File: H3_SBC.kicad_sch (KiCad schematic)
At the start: 7 parts, among them U1 H3, U8 XOS32024000LT00351005, X1 X201232768KLD2SI

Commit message: changed some ethernet stuff
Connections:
- net PA20: now reaches U1.A13 (PA20)
- net PA21: now reaches U1.A14 (PA21)
- net PA18: now reaches U1.B13 (PA18)
- net PA19: now reaches U1.B14 (PA19)
- net TWI0_SDA: now reaches U1.C13 (PA12)
- net PA17: now reaches U1.C14 (PA17)
- net JTAG_MS: now reaches U1.D11 (PA0)
- net PA9: now reaches U1.D13 (PA9)
- net UART3_CTS: now reaches U1.D15 (PA16)
- net JTAG_CK: now reaches U1.D5 (PA1)
- net JTAG_DO: now reaches U1.D6 (PA2)
- net PA7: now reaches U1.D8 (PA7)
- net PA10: now reaches U1.E11 (PA10)
- net JTAG_DI: now reaches U1.E13 (PA3)
- net PA6: now reaches U1.E14 (PA6)
- net UART3_TX: now reaches U1.E15 (PA13)
- net TWI0_SCK: now reaches U1.F11 (PA11)
- net PA8: now reaches U1.F13 (PA8)
- net UART3_RTS: now reaches U1.F14 (PA15)
- net PA4: now reaches U1.F5 (PA4)
- net UART3_RX: now reaches U1.G12 (PA14)
- net PA5: now reaches U1.H6 (PA5)
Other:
- moved on the sheet: C23, C24, C25, C26, U1A, U8, X1

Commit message: power things, minor changes
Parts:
- added D1, D3: RED, symbol Device:LED
- added D2: YELLOW, symbol Device:LED
- added R14: 47K, symbol Device:R
- added R15: 100K, symbol Device:R
- added R16, R17, R18: 330R, symbol Device:R
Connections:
- net GND: now also R16.2
- net STATLED_DISK: now reaches U1.M6 (PL9)
- net STATLED_DISK: now also R17.2
- net STATLED_ERR: now reaches U1.V2 (PL10)
- net STATLED_ERR: now also R18.2
- net at U1.AA5 (KEYADC): now also R15.2
- net at U1.AA6 (NMI): now also R14.2
- net TVOUT: now reaches U1.F10 (TVOUT)
- net AXP_PWROK: now reaches U1.V6 (RESET)
- net UBOOT: now reaches U1.W6 (UBOOT)
- net EPHY_LINK_LED: no longer names the net of U1.A2 (EPHY_LINK_LE)
- net EPHY_SPD_LED: no longer names the net of U1.F7 (EPHY_SPD_LE)
- new net: D3.1 (K), R18.1
- new net: D1.1 (K), R16.1
- new net: D2.1 (K), R17.1
- new net VCC3V3: D1.2 (A), D2.2 (A), D3.2 (A)
- new net VCC_RTC: R14.1, R15.1
- no-connect marks 7 -> 23
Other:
- moved on the sheet: C23, C24, C25, C26, U1A, U8, X1

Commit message: small changes
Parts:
- added C66: 10uF, symbol Device:C
- added C67: 0.1uF, symbol Device:C
- added C68: 1uF, symbol Device:C
- added C69: 4.7uF, symbol Device:C
- added R19: 220K, symbol Device:R
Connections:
- net GND: now also C66.2, C67.2, C68.2, C69.2, R19.2
- net PG5: now reaches U1.C1 (PG5)
- net PG4: now reaches U1.C2 (PG4)
- net PG8: now reaches U1.C3 (PG8)
- net PG11: now reaches U1.D2 (PG11)
- net PG7: now reaches U1.D3 (PG7)
- net PG9: now reaches U1.E3 (PG9)
- net PG3: now reaches U1.F3 (PG3)
- net PG6: now reaches U1.G4 (PG6)
- net PG2: now reaches U1.H4 (PG2)
- net PG0: now reaches U1.J3 (PG0)
- net PG1: now reaches U1.L2 (PG1)
- net PG10: now reaches U1.M3 (PG10)
- net at U1.V4 (VRP): now also C66.1, C67.1
- net at U1.W5 (VRA2): now also C69.1, R19.1
- net at U1.Y4 (VRA1): now also C68.1
- no-connect marks 23 -> 24
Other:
- moved on the sheet: U1B

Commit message: minor changes
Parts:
- removed U8: XOS32024000LT00351005, easyeda2kicad:OSC-SMD_4P-L3.2-W2.5-BL, symbol easyeda2kicad:XOS32024000LT00351005
- added unit 7 of U1
- added X2: SMD-5032_4P 24M 20pf, easyeda2kicad:CRYSTAL-SMD_4P-L5.0-W3.2-BL, symbol easyeda2kicad:SMD-5032_4P24M20pf
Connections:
- net GND: now also X2.2 (GND), X2.4 (GND)
- net at C25.1, U1.K2 (X24MIN): now also X2.1 (OSC1)
- net at C26.1, U1.K1 (X24MOUT): now also X2.3 (OSC2)
- new net USB0_D+: U1.A5 (USB_DP0)
- new net USB0_D-: U1.B5 (USB_DM0)
- new net USB1_D+: U1.B6 (USB_DP1)
- new net USB1_D-: U1.B7 (USB_DM1)
- new net USB2_D+: U1.A7 (USB_DP2)
- new net USB2_D-: U1.A8 (USB_DM2)
- new net USB3_D+: U1.B8 (USB_DP3)
- new net USB3_D-: U1.B9 (USB_DM3)
- no-connect marks 24 -> 40
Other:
- moved on the sheet: C23, C24, C25, C26, C66, C67, C68, C69, D1, D2, D3, R14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

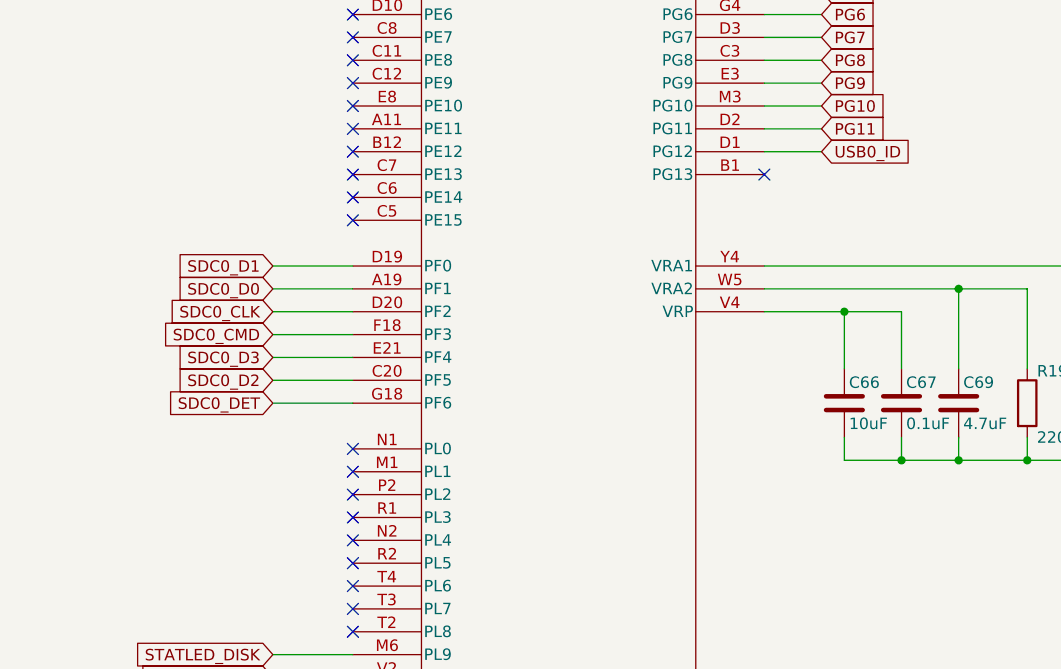
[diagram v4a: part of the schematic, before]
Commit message: recovered ethernet power changes
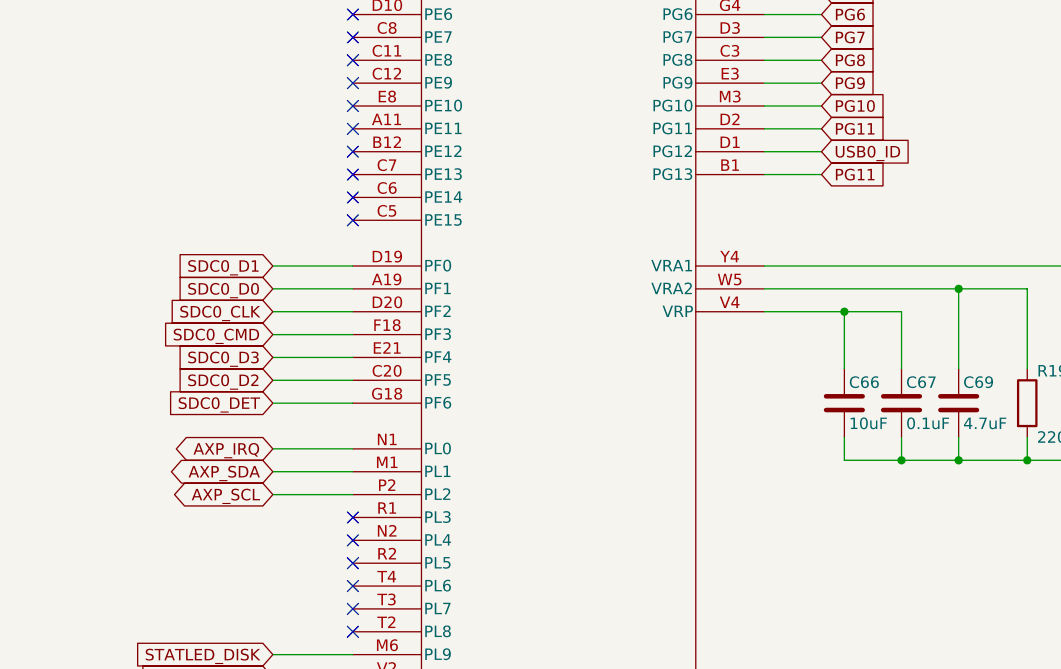
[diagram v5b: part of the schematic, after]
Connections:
- net PG11: now also U1.B1 (PG13)
- net AXP_SDA: now reaches U1.M1 (PL1)
- net AXP_IRQ: now reaches U1.N1 (PL0)
- net AXP_SCL: now reaches U1.P2 (PL2)
- no-connect marks 40 -> 36
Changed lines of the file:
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@@
-	)
-	(no_connect
-		(at 250.19 179.07)
 	)
 	(no_connect
@@
 	)
 	(no_connect
-		(at 250.19 181.61)
-	)
-	(no_connect
 		(at 68.58 96.52)
 	)
@@
 	)
 	(no_connect
-		(at 250.19 176.53)
-	)
-	(no_connect
 		(at 250.19 194.31)
 	)
@@
 	)
 	(no_connect
-		(at 295.91 146.05)
-	)
-	(no_connect
 		(at 250.19 115.57)
 	)
@@
 	(wire
 		(pts
+			(xy 295.91 146.05) (xy 302.26 146.05)
+		)
+		(stroke
+			(width 0)
+			(type default)
+		)
+	)
+	(wire
+		(pts
 			(xy 361.95 60.96) (xy 370.84 60.96)
 		)
@@
 	(wire
 		(pts
+			(xy 241.3 179.07) (xy 250.19 179.07)
+		)
+		(stroke
+			(width 0)
+			(type default)
+		)
+	)
+	(wire
+		(pts
 			(xy 304.8 161.29) (xy 304.8 167.64)
 		)
@@
 	(wire
 		(pts
+			(xy 241.3 176.53) (xy 250.19 176.53)
+		)
+		(stroke
+			(width 0)
+			(type default)
+		)
+	)
+	(wire
+		(pts
 			(xy 241.3 171.45) (xy 250.19 171.45)
 		)
@@
 	(wire
 		(pts
+			(xy 241.3 181.61) (xy 250.19 181.61)
+		)
+		(stroke
+			(width 0)
+			(type default)
+		)
+	)
+	(wire
+		(pts
 			(xy 241.3 158.75) (xy 250.19 158.75)
 		)
@@
 		)
 	)
+	(global_label "PG11"
+		(shape input)
+		(at 302.26 146.05 0)
+		(fields_autoplaced yes)
+		(effects
+			(font
+				(size 1.27 1.27)
+			)
+			(justify left)
+		)
+		(property "Intersheetrefs" "${INTERSHEET_REFS}"
+			(at 310.2042 146.05 0)
+			(effects
+				(font
+					(size 1.27 1.27)
+				)
+				(justify left)
+				(hide yes)
+			)
+		)
+	)
 	(global_label "HSCL"
 		(shape input)
@@
 		)
 	)
+	(global_label "AXP_SDA"
+		(shape bidirectional)
+		(at 241.3 179.07 180)
+		(fields_autoplaced yes)
+		(effects
+			(font
+				(size 1.27 1.27)
+			)
+			(justify right)
+		)
+		(property "Intersheetrefs" "${INTERSHEET_REFS}"
+			(at 229.0997 179.07 0)
+			(effects
+				(font
+					(size 1.27 1.27)
+				)
+				(justify right)
+				(hide yes)
+			)
+		)
+	)
 	(global_label "USB3_D-"
 		(shape input)
@@
 		)
 	)
+	(global_label "AXP_IRQ"
+		(shape bidirectional)
+		(at 241.3 176.53 180)
+		(fields_autoplaced yes)
+		(effects
+			(font
+				(size 1.27 1.27)
+			)
+			(justify right)
+		)
+		(property "Intersheetrefs" "${INTERSHEET_REFS}"
+			(at 229.4625 176.53 0)
+			(effects
+				(font
+					(size 1.27 1.27)
+				)
+				(justify right)
+				(hide yes)
+			)
+		)
+	)
 	(global_label "STATLED_DISK"
 		(shape input)
@@
 				(hide yes)
 			)
+		)
+	)
+	(global_label "AXP_SCL"
+		(shape bidirectional)
+		(at 241.3 181.61 180)
+		(fields_autoplaced yes)
+		(effects
+			(font
+				(size 1.27 1.27)
+			)
+			(justify right)
+		)
+		(property "Intersheetrefs" "${INTERSHEET_REFS}"
+			(at 229.1602 181.61 0)
+			(effects
+				(font
+					(size 1.27 1.27)
+				)
+				(justify right)
+				(hide yes)
+			)

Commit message: linking symbols to footprints
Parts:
- C23, C24, C25, C26, C68: footprint (none) -> Capacitor_SMD:C_0402_1005Metric
- C66, C67, C69: footprint (none) -> Capacitor_SMD:C_0603_1608Metric
- D1, D2, D3: footprint (none) -> LED_SMD:LED_0402_1005Metric
- R14, R15, R16, R17, R18, R19: footprint (none) -> Resistor_SMD:R_0402_1005Metric
- U1: footprint BGA347_H3_AWT -> (none)
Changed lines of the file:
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@@
 			)
 		)
-		(property "Footprint" ""
+		(property "Footprint" "Capacitor_SMD:C_0402_1005Metric"
 			(at 174.9552 87.63 0)
 			(effects
@@
 			)
 		)
-		(property "Footprint" ""
+		(property "Footprint" "Capacitor_SMD:C_0402_1005Metric"
 			(at 141.2748 96.52 0)
 			(effects
@@
 			)
 		)
-		(property "Footprint" ""
+		(property "Footprint" "Capacitor_SMD:C_0402_1005Metric"
 			(at 155.9052 113.03 0)
 			(effects
@@
 			)
 		)
-		(property "Footprint" ""
+		(property "Footprint" "Capacitor_SMD:C_0603_1608Metric"
 			(at 312.1152 175.26 0)
 			(effects
@@
 			)
 		)
-		(property "Footprint" ""
+		(property "Footprint" "LED_SMD:LED_0402_1005Metric"
 			(at 241.3 78.74 0)
 			(effects
@@
 			)
 		)
-		(property "Footprint" ""
+		(property "Footprint" "Resistor_SMD:R_0402_1005Metric"
 			(at 57.15 133.858 90)
 			(effects
@@
 			)
 		)
-		(property "Footprint" ""
+		(property "Footprint" "Resistor_SMD:R_0402_1005Metric"
 			(at 254 80.518 90)
 			(effects
@@
 			)
 		)
-		(property "Footprint" ""
+		(property "Footprint" "Capacitor_SMD:C_0402_1005Metric"
 			(at 333.7052 175.26 0)
 			(effects
@@
 			)
 		)
-		(property "Footprint" ""
+		(property "Footprint" "Capacitor_SMD:C_0603_1608Metric"
 			(at 318.4652 175.26 0)
 			(effects
@@
 			)
 		)
-		(property "Footprint" "BGA347_H3_AWT"
+		(property "Footprint" ""
 			(at 250.19 113.03 0)
 			(effects
@@
 			)
 		)
-		(property "Footprint" ""
+		(property "Footprint" "Resistor_SMD:R_0402_1005Metric"
 			(at 254 62.738 90)
 			(effects
@@
 			)
 		)
-		(property "Footprint" ""
+		(property "Footprint" "LED_SMD:LED_0402_1005Metric"
 			(at 241.3 60.96 0)
 			(effects
@@
 			)
 		)
-		(property "Footprint" "BGA347_H3_AWT"
+		(property "Footprint" ""
 			(at 68.58 71.12 0)
 			(effects
@@
 			)
 		)
-		(property "Footprint" ""
+		(property "Footprint" "Resistor_SMD:R_0402_1005Metric"
 			(at 254 71.628 90)
 			(effects
@@
 			)
 		)
-		(property "Footprint" "BGA347_H3_AWT"
+		(property "Footprint" ""
 			(at 306.07 48.26 0)
 			(effects
@@
 			)
 		)
-		(property "Footprint" ""
+		(property "Footprint" "Capacitor_SMD:C_0402_1005Metric"
 			(at 169.8752 113.03 0)
 			(effects
@@
 			)
 		)
-		(property "Footprint" ""
+		(property "Footprint" "Capacitor_SMD:C_0603_1608Metric"
 			(at 305.7652 175.26 0)
 			(effects
@@
 			)
 		)
-		(property "Footprint" ""
+		(property "Footprint" "Resistor_SMD:R_0402_1005Metric"
 			(at 323.342 171.45 90)
 			(effects
@@
 			)
 		)
-		(property "Footprint" ""
+		(property "Footprint" "LED_SMD:LED_0402_1005Metric"
 			(at 241.3 69.85 0)
 			(effects
@@
 			)
 		)
-		(property "Footprint" ""
+		(property "Footprint" "Resistor_SMD:R_0402_1005Metric"
 			(at 55.88 93.218 90)
 			(effects

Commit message: placed major components
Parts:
- C66, C67, C69: footprint Capacitor_SMD:C_0603_1608Metric -> Capacitor_SMD:C_0402_1005Metric
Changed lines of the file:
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@@
 			)
 		)
-		(property "Footprint" "Capacitor_SMD:C_0603_1608Metric"
+		(property "Footprint" "Capacitor_SMD:C_0402_1005Metric"
 			(at 312.1152 175.26 0)
 			(effects
@@
 			)
 		)
-		(property "Footprint" "Capacitor_SMD:C_0603_1608Metric"
+		(property "Footprint" "Capacitor_SMD:C_0402_1005Metric"
 			(at 318.4652 175.26 0)
 			(effects
@@
 			)
 		)
-		(property "Footprint" "Capacitor_SMD:C_0603_1608Metric"
+		(property "Footprint" "Capacitor_SMD:C_0402_1005Metric"
 			(at 305.7652 175.26 0)
 			(effects

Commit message: started RAM routing, might move to 1 module though
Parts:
- U1: footprint (none) -> easyeda2kicad:BGA-347_L14.0-W14.0-R21-C21-P0.65-TL
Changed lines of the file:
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@@
 			)
 		)
-		(property "Footprint" ""
+		(property "Footprint" "easyeda2kicad:BGA-347_L14.0-W14.0-R21-C21-P0.65-TL"
 			(at 250.19 113.03 0)
 			(effects
@@
 			)
 		)
-		(property "Footprint" ""
+		(property "Footprint" "easyeda2kicad:BGA-347_L14.0-W14.0-R21-C21-P0.65-TL"
 			(at 68.58 71.12 0)
 			(effects
@@
 			)
 		)
-		(property "Footprint" ""
+		(property "Footprint" "easyeda2kicad:BGA-347_L14.0-W14.0-R21-C21-P0.65-TL"
 			(at 306.07 48.26 0)
 			(effects
